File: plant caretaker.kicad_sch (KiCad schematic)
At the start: 1 part, among them U4 ESP32-C3

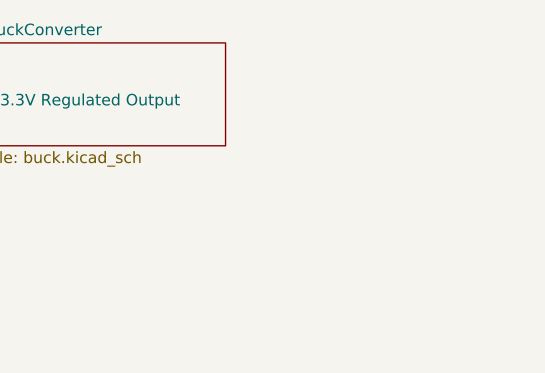
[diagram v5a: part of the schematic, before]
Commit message: Added Footprint of DJ Jack socket
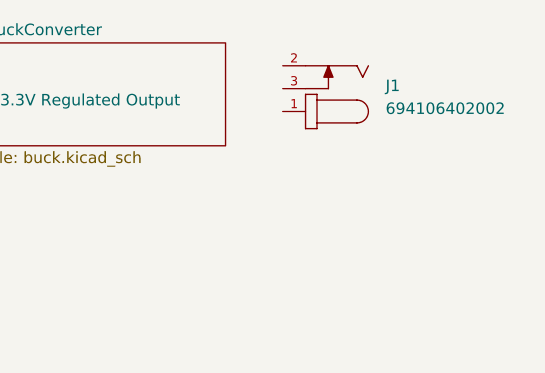
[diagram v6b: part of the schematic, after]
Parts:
- added J1: 694106402002, 694106402002:694106402002, symbol 694106402002:694106402002
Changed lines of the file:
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@@
+	)
+	(symbol
+		(lib_id "694106402002:694106402002")
+		(at 261.62 55.88 180)
+		(unit 1)
+		(exclude_from_sim no)
+		(in_bom yes)
+		(on_board yes)
+		(dnp no)
+		(fields_autoplaced yes)
+		(property "Reference" "J1"
+			(at 267.97 53.0224 0)
+			(effects
+				(font
+					(size 1.27 1.27)
+				)
+				(justify right)
+			)
+		)
+		(property "Value" "694106402002"
+			(at 267.97 55.5624 0)
+			(effects
+				(font
+					(size 1.27 1.27)
+				)
+				(justify right)
+			)
+		)
+		(property "Footprint" "694106402002:694106402002"
+			(at 261.62 55.88 0)
+			(effects
+				(font
+					(size 1.27 1.27)
+				)
+				(justify bottom)
+				(hide yes)
+			)
+		)
+		(property "Datasheet" ""
+			(at 261.62 55.88 0)
+			(effects
+				(font
+					(size 1.27 1.27)
+				)
+				(hide yes)
+			)
+		)
+		(property "Description" ""
+			(at 261.62 55.88 0)
+			(effects
+				(font
+					(size 1.27 1.27)
+				)
+				(hide yes)
+			)
+		)
+		(property "MF" "Wurth Electronics"
+			(at 261.62 55.88 0)
+			(effects
+				(font
+					(size 1.27 1.27)
+				)
+				(justify bottom)
+				(hide yes)
+			)
+		)
+		(property "Description_1" "DCPowerJack_THT_Vertical_Plastic_CenterPin_ Ø2.0"
+			(at 261.62 55.88 0)
+			(effects
+				(font
+					(size 1.27 1.27)
+				)
+				(justify bottom)
+				(hide yes)
+			)
+		)
+		(property "Package" "None"
+			(at 261.62 55.88 0)
+			(effects
+				(font
+					(size 1.27 1.27)
+				)
+				(justify bottom)
+				(hide yes)
+			)
+		)
+		(property "MOUNT" "THT"
+			(at 261.62 55.88 0)
+			(effects
+				(font
+					(size 1.27 1.27)
+				)
+				(justify bottom)
+				(hide yes)
+			)
+		)
+		(property "IR" "3A"
+			(at 261.62 55.88 0)
+			(effects
+				(font
+					(size 1.27 1.27)
+				)
+				(justify bottom)
+				(hide yes)
+			)
+		)
+		(property "VALUE" "694106402002"
+			(at 261.62 55.88 0)
+			(effects
+				(font
+					(size 1.27 1.27)
+				)
+				(justify bottom)
+				(hide yes)
+			)
+		)
+		(property "Availability" "In Stock"
+			(at 261.62 55.88 0)
+			(effects
+				(font
+					(size 1.27 1.27)
+				)
+				(justify bottom)
+				(hide yes)
+			)
+		)
+		(property "SnapEDA_Link" "https://www.snapeda.com/parts/694106402002/Wurth+Electronics/view-part/?ref=snap"
+			(at 261.62 55.88 0)
+			(effects
+				(font
+					(size 1.27 1.27)
+				)
+				(justify bottom)
+				(hide yes)
+			)
+		)
+		(property "DATASHEET-URL" "https://www.we-online.com/catalog/datasheet/694106402002.pdf"
+			(at 261.62 55.88 0)
+			(effects
+				(font
+					(size 1.27 1.27)
+				)
+				(justify bottom)
+				(hide yes)
+			)
+		)
+		(property "MP" "694106402002"
+			(at 261.62 55.88 0)
+			(effects
+				(font
+					(size 1.27 1.27)
+				)
+				(justify bottom)
+				(hide yes)
+			)
+		)
+		(property "WORKING-VOLTAGE" "20V(AC)"
+			(at 261.62 55.88 0)
+			(effects
+				(font
+					(size 1.27 1.27)
+				)
+				(justify bottom)
+				(hide yes)
+			)
+		)
+		(property "PART-NUMBER" "694106402002"
+			(at 261.62 55.88 0)
+			(effects
+				(font
+					(size 1.27 1.27)
+				)
+				(justify bottom)
+				(hide yes)
+			)
+		)
+		(property "TYPE" "Vertical"
+			(at 261.62 55.88 0)
+			(effects
+				(font
+					(size 1.27 1.27)
+				)
+				(justify bottom)
+				(hide yes)
+			)
+		)
+		(property "Price" "None"
+			(at 261.62 55.88 0)
+			(effects
+				(font
+					(size 1.27 1.27)
+				)
+				(justify bottom)
+				(hide yes)
+			)
+		)
+		(property "Check_prices" "https://www.snapeda.com/parts/694106402002/Wurth+Electronics/view-part/?ref=eda"
+			(at 261.62 55.88 0)
+			(effects
+				(font
+					(size 1.27 1.27)
+				)
+				(justify bottom)
+				(hide yes)
+			)
+		)
+		(pin "2"
+		)
+		(pin "1"
+		)
+		(pin "3"
+		)
+		(instances
+			(project ""
+				(path "/23b35dcc-615e-4aec-abee-c26cc3d8b906"
+					(reference "J1")
+					(unit 1)
+				)
+			)
+		)
 	)
 	(symbol

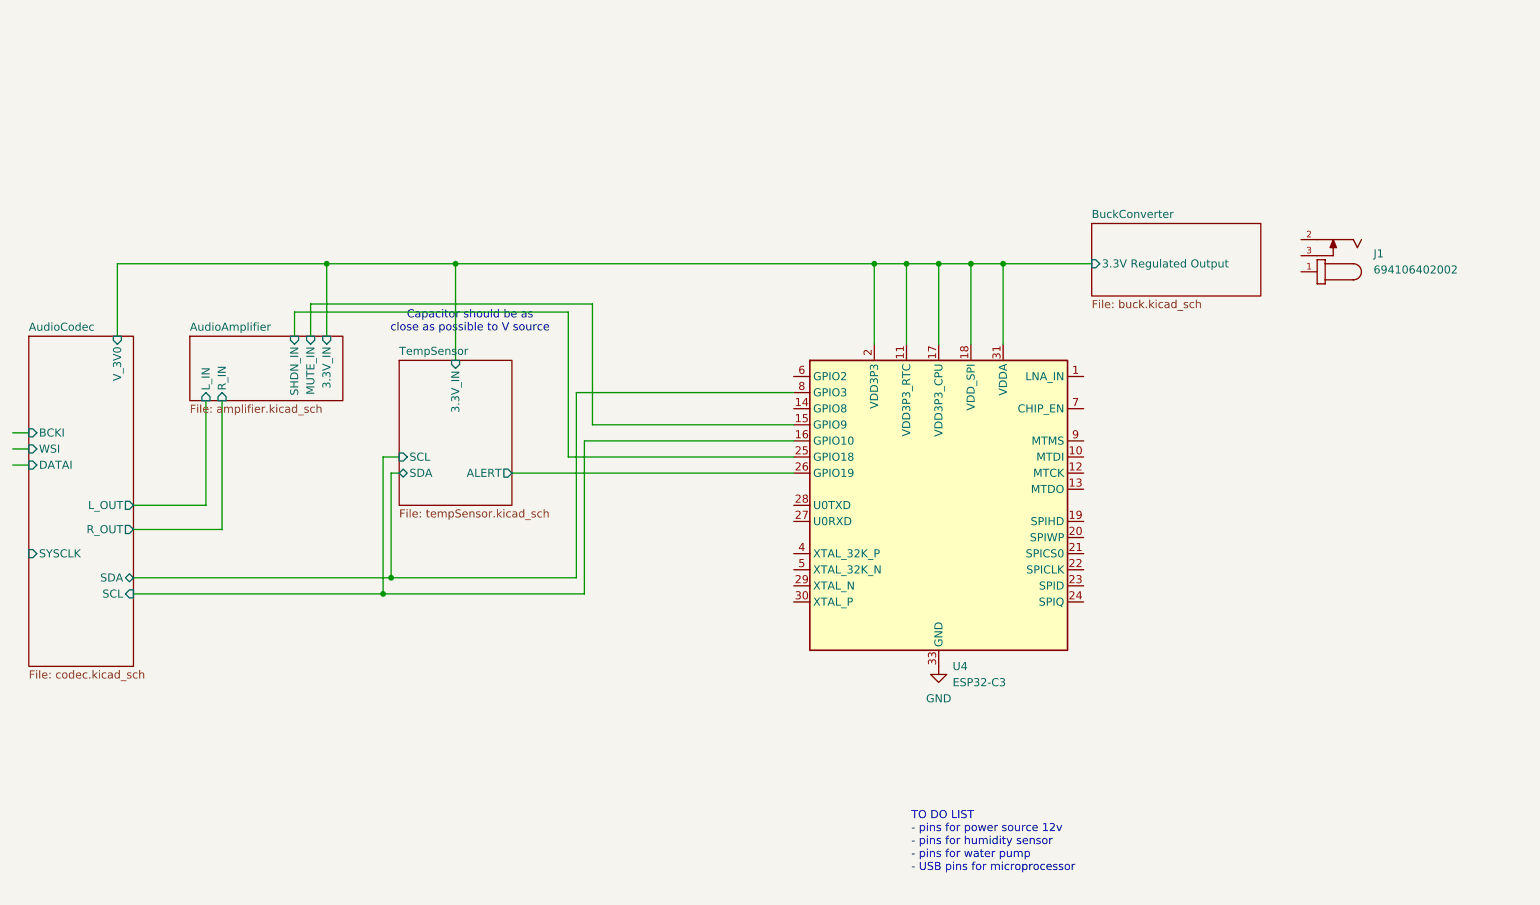
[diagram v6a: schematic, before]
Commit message: Added ESP again
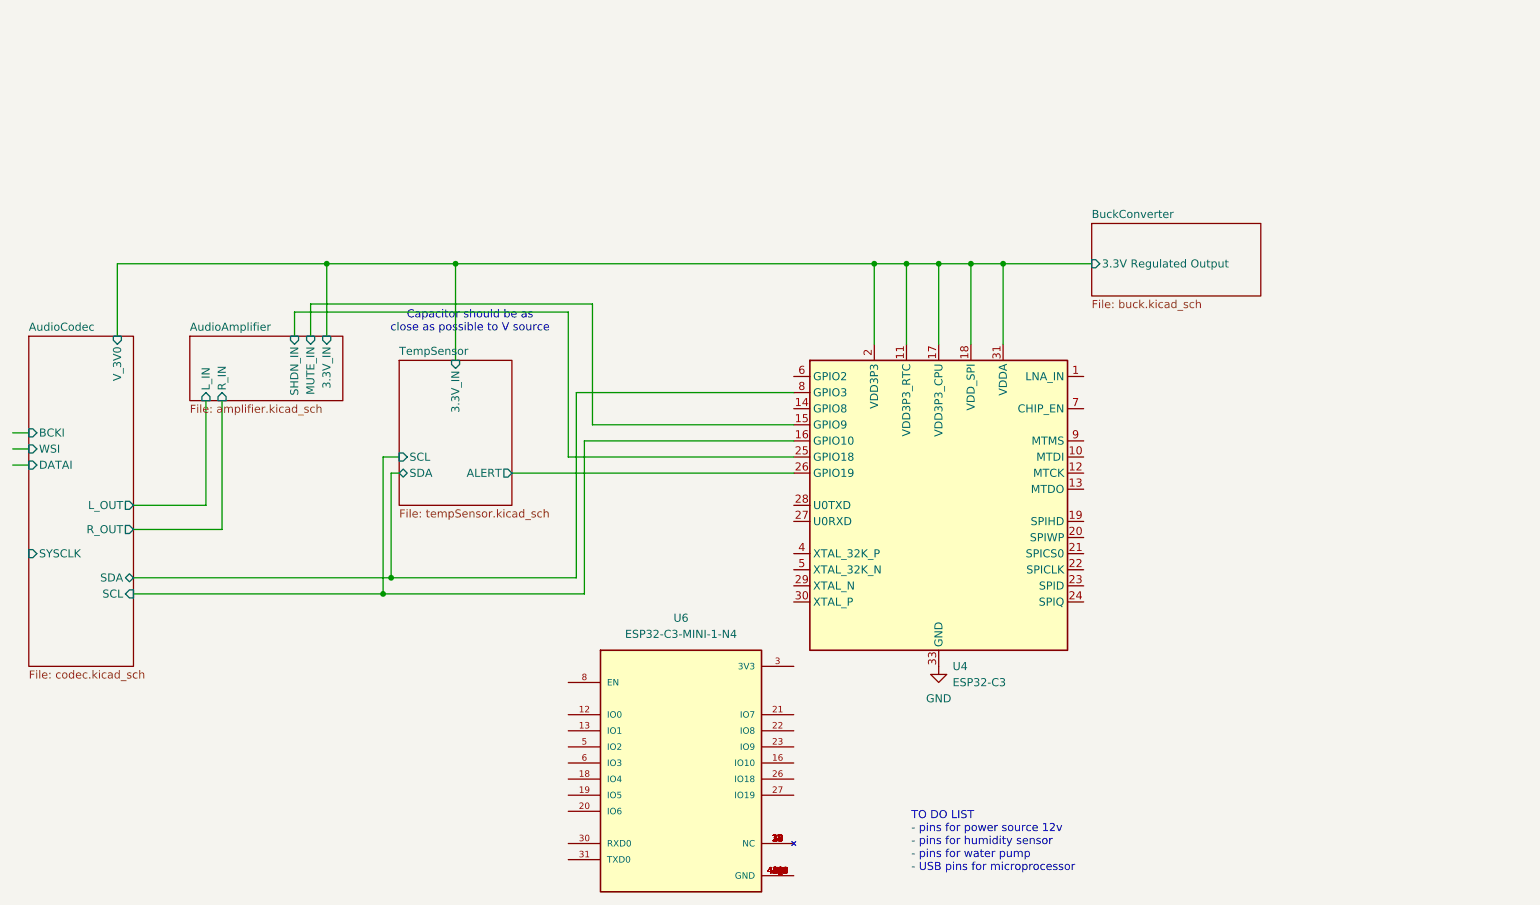
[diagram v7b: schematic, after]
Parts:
- removed J1: 694106402002, 694106402002:694106402002, symbol 694106402002:694106402002
- added U6: ESP32-C3-MINI-1-N4, a, symbol ESP32-C3-MINI-1-N4:ESP32-C3-MINI-1-N4
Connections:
- new net: U6.1 (GND), U6.11 (GND), U6.14 (GND), U6.2 (GND), U6.36 (GND), U6.37 (GND), U6.38 (GND), U6.39 (GND), U6.40 (GND), U6.41 (GND), U6.42 (GND), U6.43 (GND), U6.44 (GND), U6.45 (GND), U6.46 (GND), U6.47 (GND), U6.48 (GND), U6.49_1 (GND), U6.49_2 (GND), U6.49_3 (GND), U6.49_4 (GND), U6.49_5 (GND), U6.49_6 (GND), U6.49_7 (GND), U6.49_8 (GND), U6.49_9 (GND), U6.50 (GND), U6.51 (GND), U6.52 (GND), U6.53 (GND)
- new net: U6.10 (NC), U6.15 (NC), U6.17 (NC), U6.24 (NC), U6.25 (NC), U6.28 (NC), U6.29 (NC), U6.32 (NC), U6.33 (NC), U6.34 (NC), U6.35 (NC), U6.4 (NC), U6.7 (NC), U6.9 (NC)

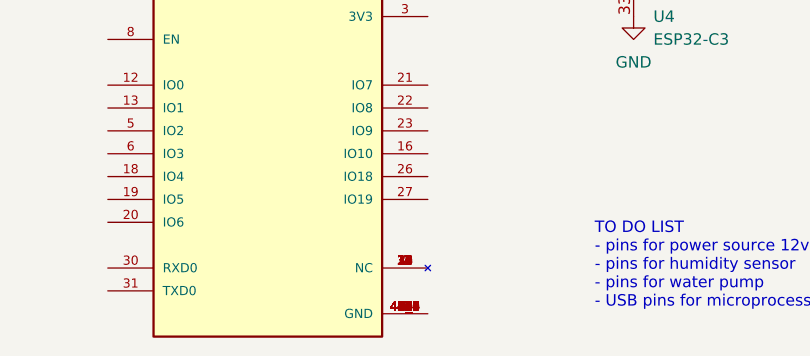
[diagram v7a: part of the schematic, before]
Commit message: Corrected pins of ESP32
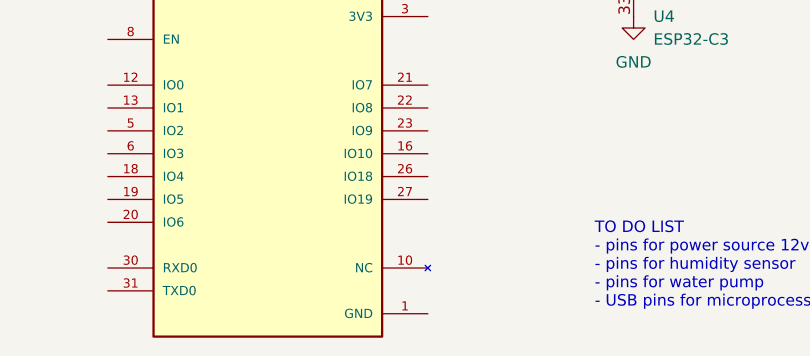
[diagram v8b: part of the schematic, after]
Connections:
- now unconnected: U6.1 (GND), U6.10 (NC)
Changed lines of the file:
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@@
 		(pin "19"
-		)
-		(pin "9"
 		)
 		(pin "8"
 		)
-		(pin "7"
-		)
 		(pin "6"
-		)
-		(pin "49_6"
-		)
-		(pin "47"
-		)
-		(pin "46"
-		)
-		(pin "48"
-		)
-		(pin "44"
-		)
-		(pin "41"
-		)
-		(pin "49_2"
-		)
-		(pin "49_3"
-		)
-		(pin "49_7"
-		)
-		(pin "49_8"
-		)
-		(pin "49_9"
-		)
-		(pin "50"
-		)
-		(pin "49_4"
-		)
-		(pin "49_5"
-		)
-		(pin "51"
-		)
-		(pin "52"
 		)
 		(pin "5"
 		)
-		(pin "40"
-		)
-		(pin "4"
-		)
-		(pin "43"
-		)
-		(pin "45"
-		)
-		(pin "42"
-		)
-		(pin "49_1"
-		)
-		(pin "38"
-		)
-		(pin "39"
-		)
 		(pin "20"
 		)
-		(pin "28"
-		)
-		(pin "32"
-		)
 		(pin "21"
-		)
-		(pin "25"
 		)
 		(pin "26"
@@
 		(pin "3"
 		)
-		(pin "53"
-		)
-		(pin "37"
-		)
-		(pin "24"
-		)
 		(pin "22"
 		)
 		(pin "27"
-		)
-		(pin "29"
 		)
 		(pin "31"
@@
 		(pin "30"
 		)
-		(pin "35"
-		)
-		(pin "36"
-		)
-		(pin "2"
-		)
-		(pin "33"
-		)
-		(pin "34"
-		)
 		(pin "23"
 		)
-		(pin "11"
-		)
 		(pin "13"
-		)
-		(pin "14"
 		)
 		(pin "10"
@@
 		(pin "16"
 		)
-		(pin "15"
-		)
 		(pin "12"
 		)
-		(pin "17"
-		)
 		(pin "18"
